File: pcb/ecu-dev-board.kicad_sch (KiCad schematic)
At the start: 0 parts

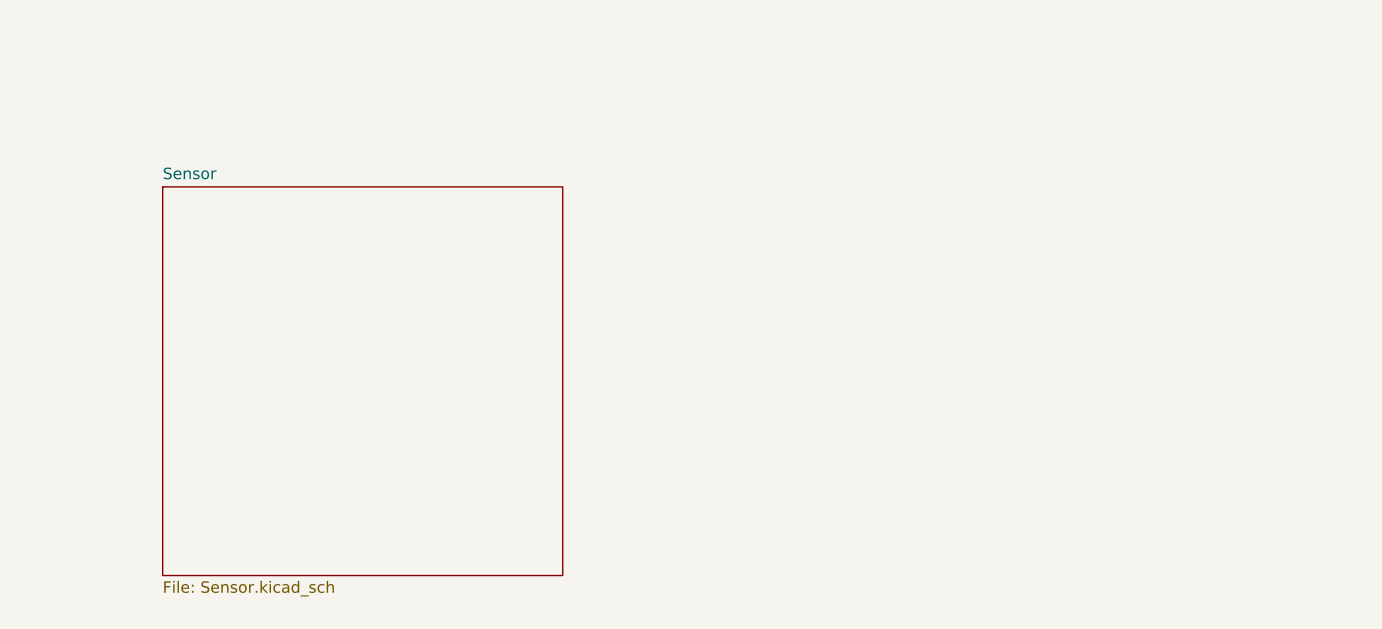
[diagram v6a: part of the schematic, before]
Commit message: added 12 to 5 buck
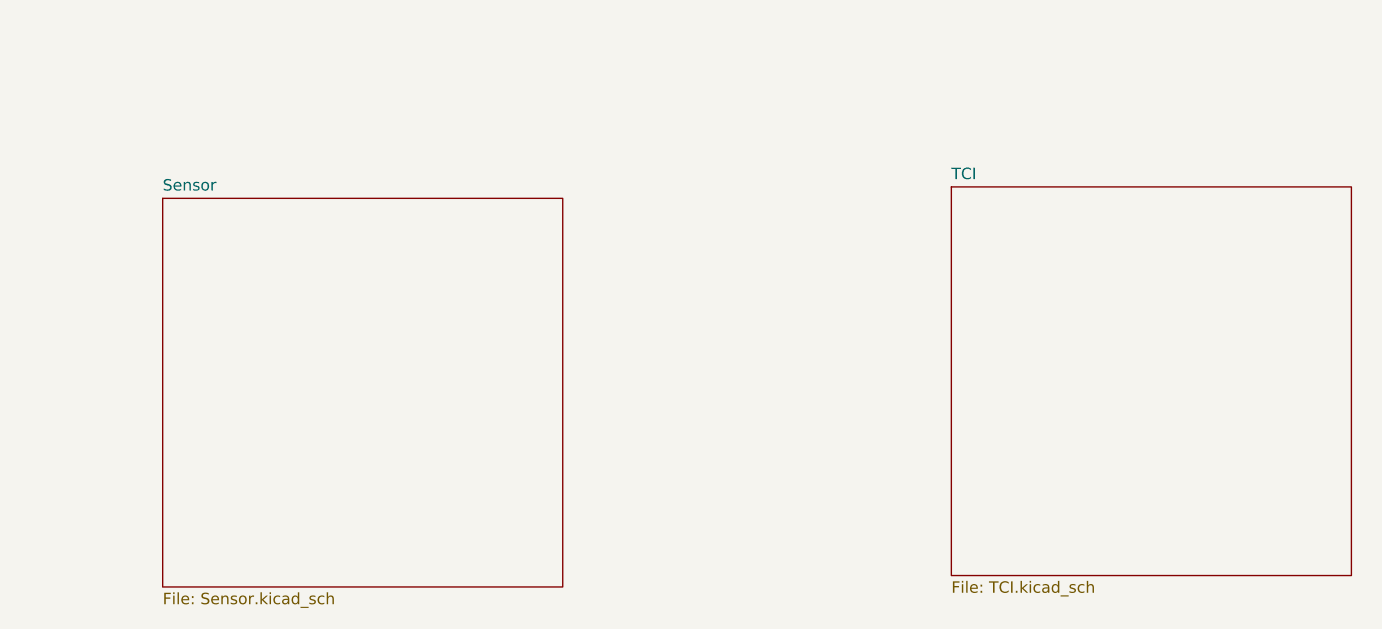
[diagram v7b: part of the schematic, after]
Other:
- added sheet TCI (TCI.kicad_sch)
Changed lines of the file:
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@@
 	(paper "A4")
+	(sheet
+		(at 217.17 95.25)
+		(size 44.45 43.18)
+		(exclude_from_sim no)
+		(in_bom yes)
+		(on_board yes)
+		(dnp no)
+		(fields_autoplaced yes)
+		(stroke
+			(width 0.1524)
+			(type solid)
+		)
+		(fill
+			(color 0 0 0 0.0000)
+		)
+		(property "Sheetname" "TCI"
+			(at 217.17 94.5384 0)
+			(effects
+				(font
+					(size 1.27 1.27)
+				)
+				(justify left bottom)
+			)
+		)
+		(property "Sheetfile" "TCI.kicad_sch"
+			(at 217.17 139.0146 0)
+			(effects
+				(font
+					(size 1.27 1.27)
+				)
+				(justify left top)
+			)
+		)
+		(instances
+			(project "ecu-dev-board"
+				(path "/38d4df77-b5a0-4642-8410-8b13c21c2c3b"
+					(page "7")
+				)
+			)
+		)
+	)
 	(sheet
 		(at 38.1 25.4)
@@
 	)
 	(sheet
-		(at 129.54 95.25)
+		(at 129.54 96.52)
 		(size 44.45 43.18)
 		(exclude_from_sim no)
@@
 		)
 		(property "Sheetname" "Sensor"
-			(at 129.54 94.5384 0)
+			(at 129.54 95.8084 0)
 			(effects
 				(font
@@
 		)
 		(property "Sheetfile" "Sensor.kicad_sch"
-			(at 129.54 139.0146 0)
+			(at 129.54 140.2846 0)
 			(effects
 				(font

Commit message: added connector and simulation link
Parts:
- added J1: MX23A18NF1, MX23A18NF1, symbol SamacSys_Parts:MX23A18NF1
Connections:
- new net COIL: J1.1
- new net GNDPWR: J1.2, J1.7
- new net KILL_SWITCH: J1.5
- new net PIEZO+: J1.12
- new net PIEZO-: J1.13
- new net SPARK: J1.18
- new net STATOR: J1.6
- new net T_COIL: J1.17
- new net VR+: J1.10
- new net VR-: J1.11
